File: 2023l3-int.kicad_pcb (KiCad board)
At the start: 2 copper layers, 180.2 x 120 mm, 44 parts, among them IC1 STM32F103CBTx, J1 0526101433, J2 52610-0833, J3 Conn_01x04, SW1 SW_DIP_x03, SW2 SW_Push, U1 DEV-15583, U10 TSSP58038, U11 TSSP58038, U12 TSSP58038, U13 TSSP58038, U14 TSSP58038, U15 TSSP58038, U16 TSSP58038, U17 TSSP58038, U18 TSSP58038, U19 TSSP58038, U2 OpenMV H7, U20 TSSP58038, U21 TSSP58038, U22 TSSP58038, U23 TSSP58038, U24 TSSP58038, U25 TSSP58038, U26 TSSP58038, U27 TSSP58038, U3 BNO085, U4 TSSP58038, U5 TSSP58038, U6 TSSP58038, U7 TSSP58038, U8 TSSP58038, U9 TSSP58038, Y1 8Mhz

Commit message: 🙏🙏🙏
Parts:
- SW1: value SW_DIP_x03 -> SW_DIP_x04; footprint Button_Switch_SMD:SW_DIP_SPSTx03_Slide_9.78x9.8mm_W8.61mm_P2.54mm -> Button_Switch_SMD:SW_DIP_SPSTx04_Slide_6.7x11.72mm_W8.61mm_P2.54mm_LowProfile
- moved SW1 0.60 mm to (180.4, 124.8)
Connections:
- SW1 pad 1: /DIP3 -> /DIP4
- SW1 pad 2: /DIP2 -> /DIP3
- SW1 pad 3: /DIP1 -> /DIP2
- SW1 pad 4: GND -> /DIP1
- U1 pad 16: unconnected-(U1-16/A2/RX4/SCL1-Pad16) -> /DIP1
- U1 pad 17: unconnected-(U1-17/A3/TX4/SDA1-Pad17) -> /DIP2
- U1 pad 20: /DIP1 -> /DIP3
- U1 pad 21: /DIP2 -> /DIP4
- U1 pad 22: /DIP3 -> unconnected-(U1-22/A8-Pad22)

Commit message: extra extension
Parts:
- added D1: LED, Connector_PinHeader_2.54mm:PinHeader_1x02_P2.54mm_Vertical, F.Cu at (192.0, 176.0)
- added R1: R_Photo, Connector_PinHeader_2.54mm:PinHeader_1x02_P2.54mm_Vertical, F.Cu at (128.0, 176.0)
- added R2: 3K24, footprints:res0603, B.Cu at (128.0, 171.8)
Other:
- board size 180.2 x 120 mm -> 180.2 x 155.6 mm

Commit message: e
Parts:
- removed R3: 10K, footprints:res0603
- removed R5: 1K, footprints:res0603
- removed SW2: SW_Push, footprints:SW_PUSH_SPST
- added REF**: MountingHole_3.2mm_M3_Pad_Via, MountingHole:MountingHole_3.2mm_M3_Pad_Via, F.Cu at (112.1, 188.2)
- added REF**: MountingHole_3.2mm_M3_Pad_Via, MountingHole:MountingHole_3.2mm_M3_Pad_Via, F.Cu at (207.9, 188.2)
- C5, C6: moved to F.Cu
- D1, R1: moved to B.Cu
- moved C5 14.8 mm to (149.7, 107.1), turned to -135 degrees
- moved R2 12.2 mm to (120.8, 181.6)
- moved C6 11.4 mm to (151.8, 109.2), turned to -135 degrees
- moved D1 10.8 mm to (202.0, 180.0), turned to 180 degrees
- moved R1 10.8 mm to (118.0, 180.0), turned to 180 degrees
- moved J1 9.50 mm to (207.5, 100.0)
- moved J2 9.50 mm to (205.6, 100.0)
- moved D2 0.71 mm to (152.5, 104.3)
- moved C2 0.42 mm to (154.6, 106.4)
- moved C1 0.22 mm to (167.8, 103.9)
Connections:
- IC1 pad 20: unconnected-(IC1-PB2-Pad20) -> /IR/IR6
- IC1 pad 21: /IR/IR6 -> unconnected-(IC1-PB10-Pad21)
- U1 pad 16: /DIP1 -> unconnected-(U1-16/A2/RX4/SCL1-Pad16)
- U1 pad 17: /DIP2 -> /DIP4
- U1 pad 21: /DIP4 -> /DIP2
- U1 pad 22: unconnected-(U1-22/A8-Pad22) -> /DIP1
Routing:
- net +5V: track 0.00 -> 171.8 mm, vias 0 -> 1
- net /IR/IR6: track 0.00 -> 83.3 mm
- net /IR/IR5: track 0.00 -> 79.4 mm
- net /IR/IR4: track 0.00 -> 63.2 mm
- net +3V3: track 3.33 -> 64.8 mm
- net /IR/IR1: track 0.00 -> 60.4 mm
- net /IR/IR3: track 0.00 -> 57.3 mm
- net /IR/IR19: track 55.8 -> 0.00 mm
- net /IR/IR23: track 0.00 -> 54.0 mm
- net /IR/IR2: track 0.00 -> 53.8 mm
- net /IR/IR24: track 0.00 -> 53.7 mm
- net /IR/IR20: track 5.55 -> 55.0 mm
- net /IR/IR21: track 5.23 -> 53.9 mm
- net /IR/IR22: track 4.48 -> 50.4 mm
- net /SDA: track 0.00 -> 38.2 mm
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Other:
- outline, holes or cut-outs redrawn
- board text removed: "RST"
- board text removed: "Use a 0.2mm Grid Sizing"

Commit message: e
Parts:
- removed REF** (x2): MountingHole_3.2mm_M3_Pad_Via, MountingHole:MountingHole_3.2mm_M3_Pad_Via
- moved R4 4.81 mm to (150.4, 97.8)
- moved C4 0.57 mm to (151.8, 96.4)
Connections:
- J3 pad 2: /IR/SWDIO -> /IR/SWCLK
- J3 pad 3: /IR/SWCLK -> /IR/SWDIO
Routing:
- net /IR/IR12: track 0.00 -> 61.5 mm
- net /IR/IR16: track 0.00 -> 60.6 mm
- net /IR/IR13: track 0.00 -> 59.4 mm
- net /IR/IR19: track 0.00 -> 55.8 mm
- net /IR/IR14: track 0.00 -> 54.5 mm
- net /IR/IR17: track 0.00 -> 54.2 mm
- net /IR/IR15: track 0.00 -> 53.4 mm
- net /IR/IR18: track 0.00 -> 52.5 mm
- net /IR/SWDIO: track 0.00 -> 17.3 mm
- net /IR/SWCLK: track 0.00 -> 15.2 mm
- net /IR/BOOT: track 0.00 -> 8.51 mm
- net +3V3: track 64.8 -> 71.6 mm
- added copper zone on B.Cu, net GND
- added copper zone on F.Cu, net GND

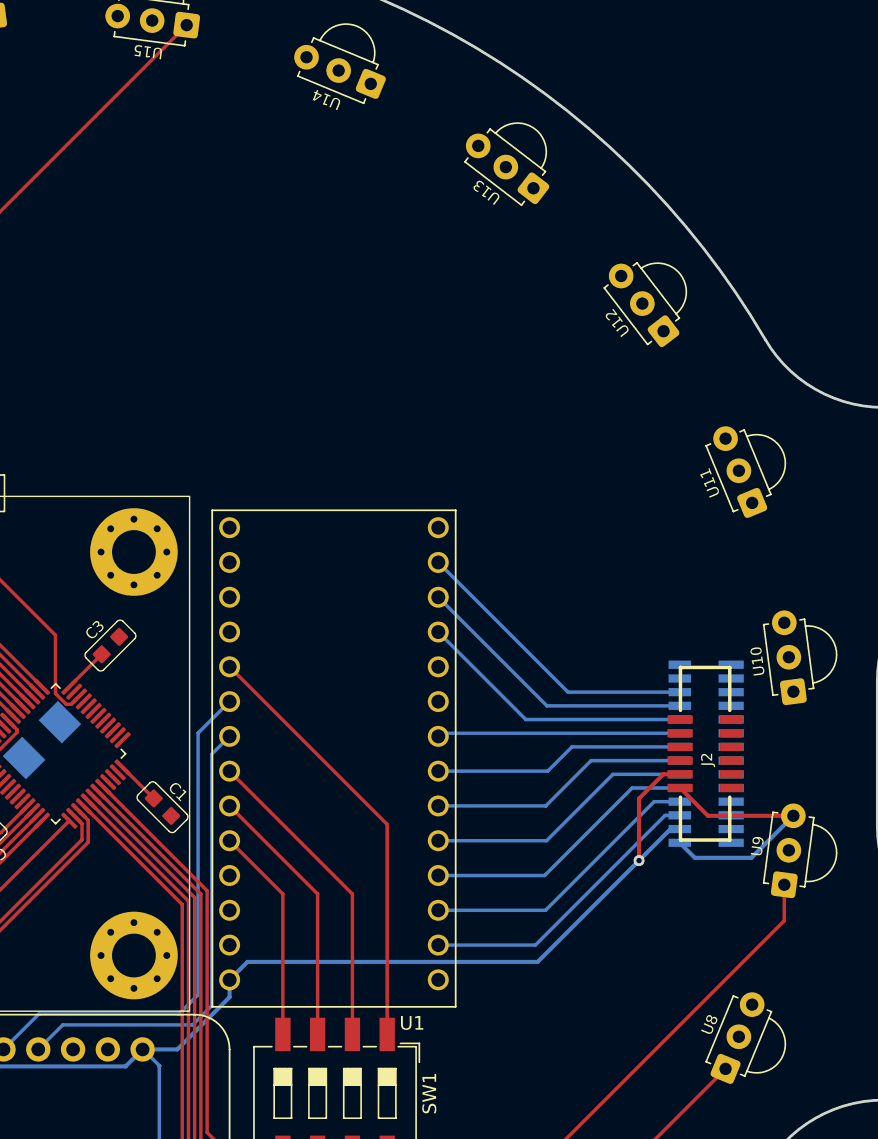
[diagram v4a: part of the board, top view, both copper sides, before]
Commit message: left with power and sw
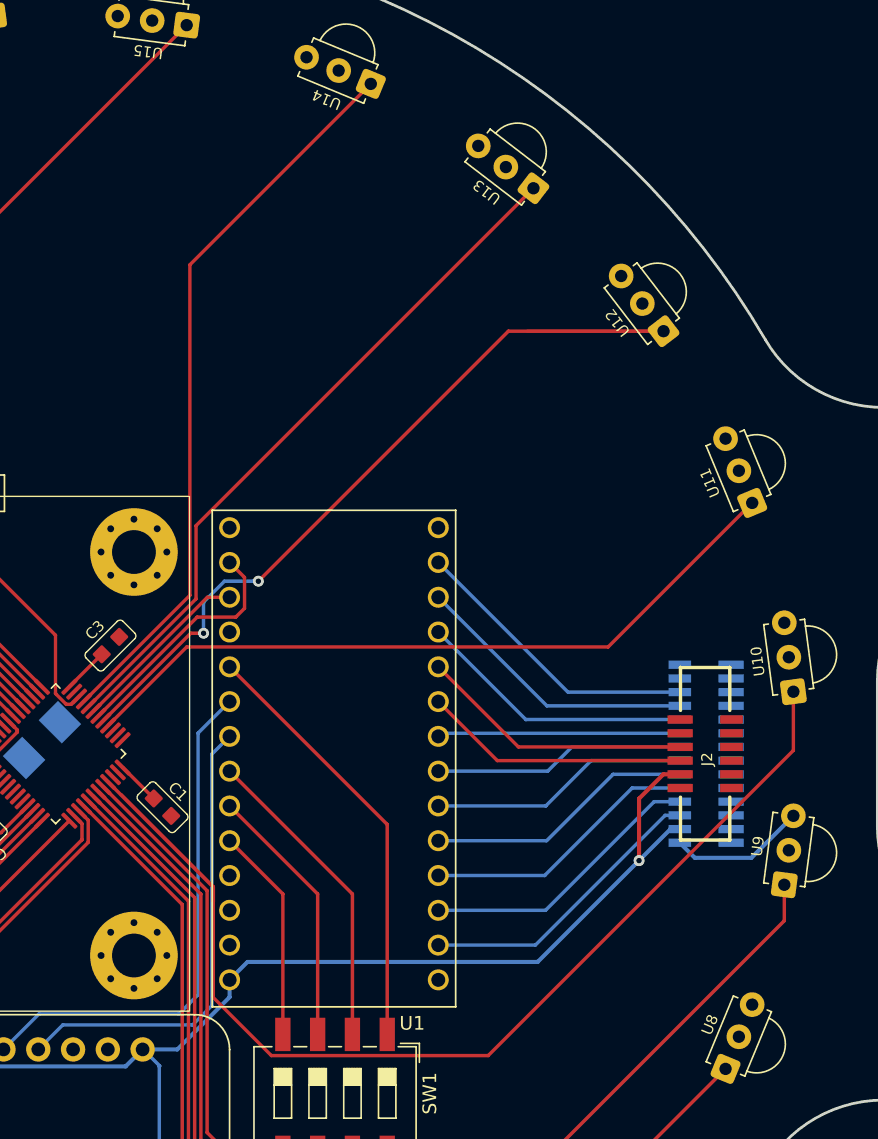
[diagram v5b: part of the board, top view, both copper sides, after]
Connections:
- IC1 pad 21: unconnected-(IC1-PB10-Pad21) -> /IR/IR7
- IC1 pad 27: /IR/IR7 -> unconnected-(IC1-PB14-Pad27)
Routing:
- net /IR/IR7: track 0.00 -> 87.1 mm
- net /IR/IR9: track 0.00 -> 64.0 mm, vias 0 -> 2
- net /IR/IR11: track 0.00 -> 53.8 mm
- net /IR/IR8: track 0.00 -> 53.8 mm
- net /IR/IR10: track 0.00 -> 51.3 mm
- net /U TX: track 0.00 -> 20.1 mm
- net /U RX: track 0.00 -> 19.4 mm
- net IR RX: track 0.00 -> 17.7 mm
- net IR TX: track 0.00 -> 13.4 mm
- net +3V3: track 71.6 -> 62.5 mm
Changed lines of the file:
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@@
   (net 106 "unconnected-(U1-16{slash}A2{slash}RX4{slash}SCL1-Pad16)")
   (net 107 "/DIP4")
-  (net 108 "unconnected-(IC1-PB10-Pad21)")
+  (net 108 "unconnected-(IC1-PB14-Pad27)")
   (footprint "footprints:Vishay_MINICAST-3P" (layer "F.Cu")
     (at 117.158919 132.873117 -52.5)
@@
       (net 34 "/IR/IR6") (pinfunction "PB2") (pintype "bidirectional"))
     (pad "21" smd roundrect (at 1.25 4.1625 45) (size 0.3 1.475) (layers "F.Cu" "F.Paste" "F.Mask") (roundrect_rratio 0.25)
-      (net 108 "unconnected-(IC1-PB10-Pad21)") (pinfunction "PB10") (pintype "bidirectional+no_connect"))
+      (net 35 "/IR/IR7") (pinfunction "PB10") (pintype "bidirectional"))
     (pad "22" smd roundrect (at 1.75 4.1625 45) (size 0.3 1.475) (layers "F.Cu" "F.Paste" "F.Mask") (roundrect_rratio 0.25)
       (net 104 "unconnected-(IC1-PB11-Pad22)") (pinfunction "PB11") (pintype "bidirectional+no_connect"))
@@
       (net 105 "unconnected-(IC1-PB13-Pad26)") (pinfunction "PB13") (pintype "bidirectional+no_connect"))
     (pad "27" smd roundrect (at 4.1625 1.75 45) (size 1.475 0.3) (layers "F.Cu" "F.Paste" "F.Mask") (roundrect_rratio 0.25)
-      (net 35 "/IR/IR7") (pinfunction "PB14") (pintype "bidirectional"))
+      (net 108 "unconnected-(IC1-PB14-Pad27)") (pinfunction "PB14") (pintype "bidirectional+no_connect"))
     (pad "28" smd roundrect (at 4.1625 1.25 45) (size 1.475 0.3) (layers "F.Cu" "F.Paste" "F.Mask") (roundrect_rratio 0.25)
       (net 36 "/IR/IR8") (pinfunction "PB15") (pintype "bidirectional"))
@@
   (segment (start 167.163604 103.263604) (end 164.898788 100.998788) (width 0.254) (layer "F.Cu") (net 3))
   (segment (start 160.998788 95.112124) (end 160.998788 95.101212) (width 0.25) (layer "F.Cu") (net 3))
-  (segment (start 205.6 102.5) (end 207.630145 104.530145) (width 0.3) (layer "F.Cu") (net 3))
   (segment (start 164.898788 100.998788) (end 164.887876 100.998788) (width 0.254) (layer "F.Cu") (net 3))
   (segment (start 157.940551 103.827215) (end 156.004162 105.763604) (width 0.254) (layer "F.Cu") (net 3))
   (segment (start 155.112124 99.001212) (end 154.401212 99.001212) (width 0.25) (layer "F.Cu") (net 3))
-  (segment (start 207.630145 104.530145) (end 213.86956 104.530145) (width 0.3) (layer "F.Cu") (net 3))
   (segment (start 160.998788 95.101212) (end 163.363604 92.736396) (width 0.25) (layer "F.Cu") (net 3))
   (segment (start 156.004162 105.763604) (end 155.236396 105.763604) (width 0.254) (layer "F.Cu") (net 3))
@@
   (segment (start 171.058 109.99734) (end 171.058 127.658) (width 0.254) (layer "F.Cu") (net 34))
   (segment (start 175.6 132.2) (end 193.2 132.2) (width 0.254) (layer "F.Cu") (net 34))
+  (segment (start 175.75 122.04) (end 171.51 117.8) (width 0.25) (layer "F.Cu") (net 35))
+  (segment (start 213.86956 99.75544) (end 191.585 122.04) (width 0.25) (layer "F.Cu") (net 35))
+  (segment (start 213.86956 95.469856) (end 213.86956 99.75544) (width 0.25) (layer "F.Cu") (net 35))
+  (segment (start 191.585 122.04) (end 175.75 122.04) (width 0.25) (layer "F.Cu") (net 35))
+  (segment (start 163.827215 102.059449) (end 171.512 109.744234) (width 0.254) (layer "F.Cu") (net 35))
+  (segment (start 171.51 117.8) (end 171.51 109.71) (width 0.25) (layer "F.Cu") (net 35))
+  (segment (start 171.51 109.71) (end 164.8 103) (width 0.25) (layer "F.Cu") (net 35))
+  (segment (start 171.512 109.744234) (end 171.512 110.8) (width 0.254) (layer "F.Cu") (net 35))
+  (segment (start 210.861511 81.681749) (end 200.34326 92.2) (width 0.25) (layer "F.Cu") (net 36))
+  (segment (start 169.567766 92.2) (end 163.827215 97.940551) (width 0.25) (layer "F.Cu") (net 36))
+  (segment (start 200.34326 92.2) (end 169.567766 92.2) (width 0.25) (layer "F.Cu") (net 36))
+  (segment (start 174.8 87.4) (end 193.058 69.142) (width 0.254) (layer "F.Cu") (net 37))
+  (segment (start 169.86066 91.2) (end 170.8 91.2) (width 0.254) (layer "F.Cu") (net 37))
+  (segment (start 163.473662 97.586998) (end 169.86066 91.2) (width 0.254) (layer "F.Cu") (net 37))
+  (segment (start 193.058 69.142) (end 204.387335 69.142) (width 0.254) (layer "F.Cu") (net 37))
+  (segment (start 194.458 69.142) (end 204.387335 69.142) (width 0.25) (layer "F.Cu") (net 37))
+  (via (at 170.8 91.2) (size 0.8) (drill 0.4) (layers "F.Cu" "B.Cu") (net 37))
+  (via (at 174.8 87.4) (size 0.8) (drill 0.4) (layers "F.Cu" "B.Cu") (net 37))
+  (segment (start 170.8 88.925678) (end 172.325678 87.4) (width 0.254) (layer "B.Cu") (net 37))
+  (segment (start 172.325678 87.4) (end 174.4 87.4) (width 0.254) (layer "B.Cu") (net 37))
+  (segment (start 170.8 91.2) (end 170.8 88.925678) (width 0.254) (layer "B.Cu") (net 37))
+  (segment (start 174.4 87.4) (end 174.8 87.4) (width 0.254) (layer "B.Cu") (net 37))
   (segment (start 161.352342 104.534322) (end 161.922279 105.104259) (width 0.254) (layer "F.Cu") (net 38))
   (segment (start 150.433315 117.766685) (end 150.433315 153.206486) (width 0.254) (layer "F.Cu") (net 38))
@@
   (segment (start 158.647658 95.465678) (end 148.675 85.49302) (width 0.25) (layer "F.Cu") (net 51))
   (segment (start 148.675 67.685199) (end 169.566685 46.793514) (width 0.25) (layer "F.Cu") (net 51))
+  (segment (start 169.8 88.432234) (end 169.8 64.294081) (width 0.25) (layer "F.Cu") (net 52))
+  (segment (start 169.8 64.294081) (end 183.01156 51.082521) (width 0.25) (layer "F.Cu") (net 52))
+  (segment (start 162.059449 96.172785) (end 169.8 88.432234) (width 0.25) (layer "F.Cu") (net 52))
+  (segment (start 170.25 88.68934) (end 162.413002 96.526338) (width 0.25) (layer "F.Cu") (net 53))
+  (segment (start 170.25 83.343409) (end 170.25 88.68934) (width 0.25) (layer "F.Cu") (net 53))
+  (segment (start 194.888235 58.705174) (end 170.25 83.343409) (width 0.25) (layer "F.Cu") (net 53))
+  (segment (start 172.7 86.03) (end 173.79 87.12) (width 0.25) (layer "F.Cu") (net 58))
+  (segment (start 173.151493 90.02) (end 170.333554 90.02) (width 0.25) (layer "F.Cu") (net 58))
+  (segment (start 173.79 89.381493) (end 173.151493 90.02) (width 0.25) (layer "F.Cu") (net 58))
+  (segment (start 170.333554 90.02) (end 163.120109 97.233445) (width 0.25) (layer "F.Cu") (net 58))
+  (segment (start 173.79 87.12) (end 173.79 89.381493) (width 0.25) (layer "F.Cu") (net 58))
+  (segment (start 171.076446 88.57) (end 172.7 88.57) (width 0.25) (layer "F.Cu") (net 59))
+  (segment (start 162.766555 96.879891) (end 171.076446 88.57) (width 0.25) (layer "F.Cu") (net 59))
   (segment (start 176.59 120.495) (end 176.59 110.24) (width 0.254) (layer "F.Cu") (net 60))
   (segment (start 176.59 110.24) (end 172.7 106.35) (width 0.254) (layer "F.Cu") (net 60))
@@
   (segment (start 181.67 120.495) (end 181.67 110.24) (width 0.254) (layer "F.Cu") (net 62))
   (segment (start 181.67 110.24) (end 172.7 101.27) (width 0.254) (layer "F.Cu") (net 62))
+  (segment (start 193.79 99.5) (end 187.94 93.65) (width 0.25) (layer "F.Cu") (net 95))
+  (segment (start 205.6 99.5) (end 193.79 99.5) (width 0.25) (layer "F.Cu") (net 95))
+  (segment (start 192.25 100.5) (end 205.6 100.5) (width 0.25) (layer "F.Cu") (net 97))
+  (segment (start 187.94 96.19) (end 192.25 100.5) (width 0.25) (layer "F.Cu") (net 97))
   (segment (start 172.7 93.65) (end 184.21 105.16) (width 0.254) (layer "F.Cu") (net 107))
   (segment (start 184.21 105.16) (end 184.21 120.495) (width 0.254) (layer "F.Cu") (net 107))

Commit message: i wanna kill myself
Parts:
- added R3: 10K, footprints:res0603, F.Cu at (150.8, 108.2)
- added R5: 1K, footprints:res0603, F.Cu at (142.4, 108.2)
- added SW2: SW_Push, footprints:SW_PUSH_SPST, F.Cu at (146.6, 108.2)
- C5, C6: moved to B.Cu
- J1: footprint footprints:526101433 -> footprints:522711479
- moved J1 18.5 mm to (226.0, 100.0), turned to -90 degrees
- moved C6 17.6 mm to (164.8, 97.4), turned to 45 degrees
- moved C5 17.5 mm to (162.2, 94.8), turned to 45 degrees
- moved Y1 2.00 mm to (161.0, 99.0), turned to 135 degrees
- moved R4 0.57 mm to (150.0, 98.2)
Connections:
- D1 pad 2: +5V -> +3V3
- J1 pad 1: unconnected-(J1-Pad1) -> GND
- J1 pad 11: unconnected-(J1-Pad11) -> /L1 TX
- J1 pad 12: /FL DIR -> /L1 RX
- J1 pad 13: unconnected-(J1-Pad13) -> +5V
- J1 pad 14: /FR PWM -> +3V3
- J1 pad 2: +3V3 -> GND
- J1 pad 3: unconnected-(J1-Pad3) -> /BR DIR
- J1 pad 4: +5V -> /BR PWM
- J1 pad 5: unconnected-(J1-Pad5) -> /BL DIR
- J1 pad 6: /L1 RX -> /BL PWM
- J1 pad 7: unconnected-(J1-Pad7) -> /FR DIR
- J1 pad 8: /L1 TX -> /FR PWM
- J1 pad 9: unconnected-(J1-Pad9) -> /FL DIR
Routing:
- net +3V3: track 62.5 -> 604.3 mm, vias 0 -> 3
- net /LG: track 2.82 -> 120.4 mm, vias 0 -> 2
- net +5V: track 171.8 -> 113.6 mm
- net /FL DIR: track 19.6 -> 37.0 mm
- net /L1 RX: track 21.6 -> 38.7 mm
- net /BR DIR: track 21.6 -> 38.4 mm
- net /L1 TX: track 20.9 -> 37.6 mm
- net /BR PWM: track 20.9 -> 37.3 mm
- net /FL PWM: track 20.3 -> 36.5 mm
- net /BL DIR: track 20.3 -> 36.3 mm
- net /FR PWM: track 19.0 -> 34.9 mm
- net /FR DIR: track 18.4 -> 34.1 mm
- net /BL PWM: track 17.7 -> 33.5 mm
- net /IR/RST: track 0.00 -> 10.7 mm
- net Net-(IC1-PD1): track 0.00 -> 9.49 mm, vias 0 -> 1
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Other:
- outline, holes or cut-outs redrawn

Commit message: i wanna kill myself
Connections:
- IC1 pad 30: IR RX -> /IR/IR RX
- IC1 pad 31: IR TX -> /IR/IR TX
- U1 pad 12: unconnected-(U1-12/MISO-Pad12) -> /DIP4
- U1 pad 14: IR RX -> /IR RX
- U1 pad 15: IR TX -> /IR TX
- U1 pad 16: unconnected-(U1-16/A2/RX4/SCL1-Pad16) -> /C RX
- U1 pad 17: /DIP4 -> /C TX
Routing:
- net /C RX: track 0.00 -> 50.3 mm
- net /C TX: track 0.00 -> 47.5 mm
- net IR RX: track 17.7 -> 0.00 mm
- net /IR RX: track 0.00 -> 17.7 mm
- net +3V3: track 604.3 -> 618.4 mm
- net IR TX: track 13.4 -> 0.00 mm
- net /IR TX: track 0.00 -> 13.4 mm
- net /IR/IR3: track 57.3 -> 68.7 mm
- net /IR/IR7: track 88.6 -> 78.0 mm
- net /IR/IR2: track 53.8 -> 61.5 mm
- net /DIP4: track 31.6 -> 38.6 mm, vias 0 -> 1
- net /IR/IR5: track 79.4 -> 73.0 mm
- net /FL DIR: track 37.0 -> 35.8 mm

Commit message: kill me
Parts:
- added H1: MountingHole_Pad, MountingHole:MountingHole_3.2mm_M3_Pad_Via, F.Cu at (111.6, 188.2)
- added H2: MountingHole_Pad, MountingHole:MountingHole_3.2mm_M3_Pad_Via, F.Cu at (208.4, 188.2)
- added H3: MountingHole_Pad, MountingHole:MountingHole_3.2mm_M3_Pad_Via, F.Cu at (74.9, 120.3)
- added H4: MountingHole_Pad, MountingHole:MountingHole_3.2mm_M3_Pad_Via, F.Cu at (245.1, 120.3)
- added H5: MountingHole_Pad, MountingHole:MountingHole_3.2mm_M3_Pad_Via, F.Cu at (245.1, 79.7)
- added H6: MountingHole_Pad, MountingHole:MountingHole_3.2mm_M3_Pad_Via, F.Cu at (74.9, 79.7)
- moved C3 0.50 mm to (163.6, 91.8)
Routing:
- net /IR/BOOT: track 8.75 -> 33.4 mm, vias 0 -> 2
- net /IR/IR9: track 64.0 -> 54.0 mm
- net /IR/SWDIO: track 17.3 -> 22.9 mm
- net +3V3: track 618.4 -> 619.3 mm
- net /IR/IR21: track 53.9 -> 54.7 mm
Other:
- board text added: "3V3"
- board text added: "5V"
- board text added: "KEEP HANDS OFF"
- board text added: "RX"
- board text added: "TX"
- board text removed: "PWR"
